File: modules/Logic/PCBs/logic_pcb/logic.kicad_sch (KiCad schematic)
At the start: 14 parts, among them U1 CD74HCT132E, U2 CD74HCT132E, U3 LM324

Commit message: Switch ALU to SMD components
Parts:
- C1: footprint Capacitor_THT:C_Disc_D4.7mm_W2.5mm_P5.00mm -> Capacitor_SMD:C_0805_2012Metric_Pad1.18x1.45mm_HandSolder; JLC (none) -> C376974
- R1, R10, R2, R6, R7, R9: footprint Resistor_THT:R_Axial_DIN0207_L6.3mm_D2.5mm_P10.16mm_Horizontal -> Resistor_SMD:R_0805_2012Metric_Pad1.20x1.40mm_HandSolder; JLC (none) -> C17414
- R3, R4, R5, R8: footprint Resistor_THT:R_Axial_DIN0207_L6.3mm_D2.5mm_P10.16mm_Horizontal -> Resistor_SMD:R_0805_2012Metric_Pad1.20x1.40mm_HandSolder; JLC (none) -> C17513
- U1, U2: footprint Package_DIP:DIP-14_W7.62mm -> Package_SO:SOIC-14_3.9x8.7mm_P1.27mm; JLC (none) -> C484714
- U3: footprint Package_DIP:DIP-14_W7.62mm -> Package_SO:SOIC-14_3.9x8.7mm_P1.27mm; JLC (none) -> C7943
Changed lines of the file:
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@@
 		(shape output)
 		(at 151.13 139.7 0)
-		(fields_autoplaced yes)
 		(effects
 			(font
@@
 		(shape input)
 		(at 38.1 31.75 180)
-		(fields_autoplaced yes)
 		(effects
 			(font
@@
 		(shape output)
 		(at 129.54 95.25 0)
-		(fields_autoplaced yes)
 		(effects
 			(font
@@
 		(shape output)
 		(at 111.76 43.18 0)
-		(fields_autoplaced yes)
 		(effects
 			(font
@@
 		(shape input)
 		(at 92.71 97.79 180)
-		(fields_autoplaced yes)
 		(effects
 			(font
@@
 		(shape input)
 		(at 93.98 118.11 270)
-		(fields_autoplaced yes)
 		(effects
 			(font
@@
 		(shape output)
 		(at 128.27 59.69 0)
-		(fields_autoplaced yes)
 		(effects
 			(font
@@
 		(shape input)
 		(at 38.1 49.53 180)
-		(fields_autoplaced yes)
 		(effects
 			(font
@@
 			)
 		)
-		(property "Footprint" "Resistor_THT:R_Axial_DIN0207_L6.3mm_D2.5mm_P10.16mm_Horizontal"
+		(property "Footprint" "Resistor_SMD:R_0805_2012Metric_Pad1.20x1.40mm_HandSolder"
 			(at 146.05 141.478 90)
 			(effects
@@
 		)
 		(property "Description" "Resistor"
+			(at 146.05 139.7 0)
+			(effects
+				(font
+					(size 1.27 1.27)
+				)
+				(hide yes)
+			)
+		)
+		(property "JLC" "C17513"
 			(at 146.05 139.7 0)
 			(effects
@@
 			)
 		)
-		(property "Footprint" "Package_DIP:DIP-14_W7.62mm"
+		(property "Footprint" "Package_SO:SOIC-14_3.9x8.7mm_P1.27mm"
 			(at 71.12 139.7 0)
 			(effects
@@
 		)
 		(property "Description" "quad 2-input NAND gate"
+			(at 71.12 139.7 0)
+			(effects
+				(font
+					(size 1.27 1.27)
+				)
+				(hide yes)
+			)
+		)
+		(property "JLC" "C484714"
 			(at 71.12 139.7 0)
 			(effects
@@
 			)
 		)
-		(property "Footprint" "Resistor_THT:R_Axial_DIN0207_L6.3mm_D2.5mm_P10.16mm_Horizontal"
+		(property "Footprint" "Resistor_SMD:R_0805_2012Metric_Pad1.20x1.40mm_HandSolder"
 			(at 43.18 33.528 90)
 			(effects
@@
 		)
 		(property "Description" "Resistor"
+			(at 43.18 31.75 0)
+			(effects
+				(font
+					(size 1.27 1.27)
+				)
+				(hide yes)
+			)
+		)
+		(property "JLC" "C17414"
 			(at 43.18 31.75 0)
 			(effects
@@
 			)
 		)
-		(property "Footprint" "Package_DIP:DIP-14_W7.62mm"
+		(property "Footprint" "Package_SO:SOIC-14_3.9x8.7mm_P1.27mm"
 			(at 71.12 34.29 0)
 			(effects
@@
 		)
 		(property "Description" "quad 2-input NAND gate"
+			(at 71.12 34.29 0)
+			(effects
+				(font
+					(size 1.27 1.27)
+				)
+				(hide yes)
+			)
+		)
+		(property "JLC" "C484714"
 			(at 71.12 34.29 0)
 			(effects
@@
 			)
 		)
-		(property "Footprint" "Package_DIP:DIP-14_W7.62mm"
+		(property "Footprint" "Package_SO:SOIC-14_3.9x8.7mm_P1.27mm"
 			(at 110.49 59.69 0)
 			(effects
@@
 		)
 		(property "Description" "quad 2-input NAND gate"
+			(at 110.49 59.69 0)
+			(effects
+				(font
+					(size 1.27 1.27)
+				)
+				(hide yes)
+			)
+		)
+		(property "JLC" "C484714"
 			(at 110.49 59.69 0)
 			(effects
@@
 			)
 		)
-		(property "Footprint" "Package_DIP:DIP-14_W7.62mm"
+		(property "Footprint" "Package_SO:SOIC-14_3.9x8.7mm_P1.27mm"
 			(at 111.76 148.59 0)
 			(effects
@@
 		)
 		(property "Description" "quad 2-input NAND gate"
+			(at 111.76 148.59 0)
+			(effects
+				(font
+					(size 1.27 1.27)
+				)
+				(hide yes)
+			)
+		)
+		(property "JLC" "C484714"
 			(at 111.76 148.59 0)
 			(effects
@@
 			)
 		)
-		(property "Footprint" "Capacitor_THT:C_Disc_D4.7mm_W2.5mm_P5.00mm"
+		(property "Footprint" "Capacitor_SMD:C_0805_2012Metric_Pad1.18x1.45mm_HandSolder"
 			(at 115.57 85.3948 0)
 			(effects
@@
 		)
 		(property "Description" "Unpolarized capacitor"
+			(at 111.76 86.36 0)
+			(effects
+				(font
+					(size 1.27 1.27)
+				)
+				(hide yes)
+			)
+		)
+		(property "JLC" "C376974"
 			(at 111.76 86.36 0)
 			(effects
@@
 			)
 		)
-		(property "Footprint" "Package_DIP:DIP-14_W7.62mm"
+		(property "Footprint" "Package_SO:SOIC-14_3.9x8.7mm_P1.27mm"
 			(at 133.35 139.7 0)
 			(effects
@@
 		)
 		(property "Description" "quad 2-input NAND gate"
+			(at 133.35 139.7 0)
+			(effects
+				(font
+					(size 1.27 1.27)
+				)
+				(hide yes)
+			)
+		)
+		(property "JLC" "C484714"
 			(at 133.35 139.7 0)
 			(effects
@@
 			)
 		)
-		(property "Footprint" "Resistor_THT:R_Axial_DIN0207_L6.3mm_D2.5mm_P10.16mm_Horizontal"
+		(property "Footprint" "Resistor_SMD:R_0805_2012Metric_Pad1.20x1.40mm_HandSolder"
 			(at 123.19 61.468 90)
 			(effects
@@
 		)
 		(property "Description" "Resistor"
+			(at 123.19 59.69 0)
+			(effects
+				(font
+					(size 1.27 1.27)
+				)
+				(hide yes)
+			)
+		)
+		(property "JLC" "C17513"
 			(at 123.19 59.69 0)
 			(effects
@@
 			)
 		)
-		(property "Footprint" "Resistor_THT:R_Axial_DIN0207_L6.3mm_D2.5mm_P10.16mm_Horizontal"
+		(property "Footprint" "Resistor_SMD:R_0805_2012Metric_Pad1.20x1.40mm_HandSolder"
 			(at 124.46 97.028 90)
 			(effects
@@
 		)
 		(property "Description" "Resistor"
+			(at 124.46 95.25 0)
+			(effects
+				(font
+					(size 1.27 1.27)
+				)
+				(hide yes)
+			)
+		)
+		(property "JLC" "C17513"
 			(at 124.46 95.25 0)
 			(effects
@@
 			)
 		)
-		(property "Footprint" "Resistor_THT:R_Axial_DIN0207_L6.3mm_D2.5mm_P10.16mm_Horizontal"
+		(property "Footprint" "Resistor_SMD:R_0805_2012Metric_Pad1.20x1.40mm_HandSolder"
 			(at 95.758 102.87 90)
 			(effects
@@
 		)
 		(property "Description" "Resistor"
+			(at 93.98 102.87 0)
+			(effects
+				(font
+					(size 1.27 1.27)
+				)
+				(hide yes)
+			)
+		)
+		(property "JLC" "C17414"
 			(at 93.98 102.87 0)
 			(effects
@@
 			)
 		)
-		(property "Footprint" "Resistor_THT:R_Axial_DIN0207_L6.3mm_D2.5mm_P10.16mm_Horizontal"
+		(property "Footprint" "Resistor_SMD:R_0805_2012Metric_Pad1.20x1.40mm_HandSolder"
 			(at 111.76 77.978 90)
 			(effects
@@
 		)
 		(property "Description" "Resistor"
+			(at 111.76 76.2 0)
+			(effects
+				(font
+					(size 1.27 1.27)
+				)
+				(hide yes)
+			)
+		)
+		(property "JLC" "C17414"
 			(at 111.76 76.2 0)
 			(effects
@@
 			)
 		)
-		(property "Footprint" "Package_DIP:DIP-14_W7.62mm"
+		(property "Footprint" "Package_SO:SOIC-14_3.9x8.7mm_P1.27mm"
 			(at 92.71 43.18 0)
 			(effects
@@
 		)
 		(property "Description" "quad 2-input NAND gate"
+			(at 92.71 43.18 0)
+			(effects
+				(font
+					(size 1.27 1.27)
+				)
+				(hide yes)
+			)
+		)
+		(property "JLC" "C484714"
 			(at 92.71 43.18 0)
 			(effects
@@
 			)
 		)
-		(property "Footprint" "Resistor_THT:R_Axial_DIN0207_L6.3mm_D2.5mm_P10.16mm_Horizontal"
+		(property "Footprint" "Resistor_SMD:R_0805_2012Metric_Pad1.20x1.40mm_HandSolder"
 			(at 43.18 51.308 90)
 			(effects
@@
 		)
 		(property "Description" "Resistor"
+			(at 43.18 49.53 0)
+			(effects
+				(font
+					(size 1.27 1.27)
+				)
+				(hide yes)
+			)
+		)
+		(property "JLC" "C17414"
 			(at 43.18 49.53 0)
 			(effects
@@
 			)
 		)
-		(property "Footprint" "Package_DIP:DIP-14_W7.62mm"
+		(property "Footprint" "Package_SO:SOIC-14_3.9x8.7mm_P1.27mm"
 			(at 111.76 130.81 0)
 			(effects
@@
 		)
 		(property "Description" "quad 2-input NAND gate"
+			(at 111.76 130.81 0)
+			(effects
+				(font
+					(size 1.27 1.27)
+				)
+				(hide yes)
+			)
+		)
+		(property "JLC" "C484714"
 			(at 111.76 130.81 0)
 			(effects
@@
 			)
 		)
-		(property "Footprint" "Resistor_THT:R_Axial_DIN0207_L6.3mm_D2.5mm_P10.16mm_Horizontal"
+		(property "Footprint" "Resistor_SMD:R_0805_2012Metric_Pad1.20x1.40mm_HandSolder"
 			(at 106.68 44.958 90)
 			(effects
@@
 		)
 		(property "Description" "Resistor"
+			(at 106.68 43.18 0)
+			(effects
+				(font
+					(size 1.27 1.27)
+				)
+				(hide yes)
+			)
+		)
+		(property "JLC" "C17513"
 			(at 106.68 43.18 0)
 			(effects
@@
 			)
 		)
-		(property "Footprint" "Package_DIP:DIP-14_W7.62mm"
+		(property "Footprint" "Package_SO:SOIC-14_3.9x8.7mm_P1.27mm"
 			(at 71.12 52.07 0)
 			(effects
@@
 		)
 		(property "Description" "quad 2-input NAND gate"
+			(at 71.12 52.07 0)
+			(effects
+				(font
+					(size 1.27 1.27)
+				)
+				(hide yes)
+			)
+		)
+		(property "JLC" "C484714"
 			(at 71.12 52.07 0)
 			(effects
@@
 			)
 		)
-		(property "Footprint" "Package_DIP:DIP-14_W7.62mm"
+		(property "Footprint" "Package_SO:SOIC-14_3.9x8.7mm_P1.27mm"
 			(at 110.49 97.79 0)
 			(effects
@@
 		)
 		(property "Description" "Low-Power, Quad-Operational Amplifiers, DIP-14/SOIC-14/SSOP-14"
+			(at 111.76 95.25 0)
+			(effects
+				(font
+					(size 1.27 1.27)
+				)
+				(hide yes)
+			)
+		)
+		(property "JLC" "C7943"
 			(at 111.76 95.25 0)
 			(effects
@@
 			)
 		)
-		(property "Footprint" "Resistor_THT:R_Axial_DIN0207_L6.3mm_D2.5mm_P10.16mm_Horizontal"
+		(property "Footprint" "Resistor_SMD:R_0805_2012Metric_Pad1.20x1.40mm_HandSolder"
 			(at 97.79 94.488 90)
 			(effects
@@
 		)
 		(property "Description" "Resistor"
+			(at 97.79 92.71 0)
+			(effects
+				(font
+					(size 1.27 1.27)
+				)
+				(hide yes)
+			)
+		)
+		(property "JLC" "C17414"
 			(at 97.79 92.71 0)
 			(effects
@@
 			)
 		)
-		(property "Footprint" "Resistor_THT:R_Axial_DIN0207_L6.3mm_D2.5mm_P10.16mm_Horizontal"
+		(property "Footprint" "Resistor_SMD:R_0805_2012Metric_Pad1.20x1.40mm_HandSolder"
 			(at 95.758 113.03 90)
 			(effects
@@
 			(at 93.98 113.03 0)
 			(effects
+				(font
+					(size 1.27 1.27)
+				)
+				(hide yes)
+			)
+		)
+		(property "JLC" "C17414"
+			(at 93.98 113.03 0)
+			(effects

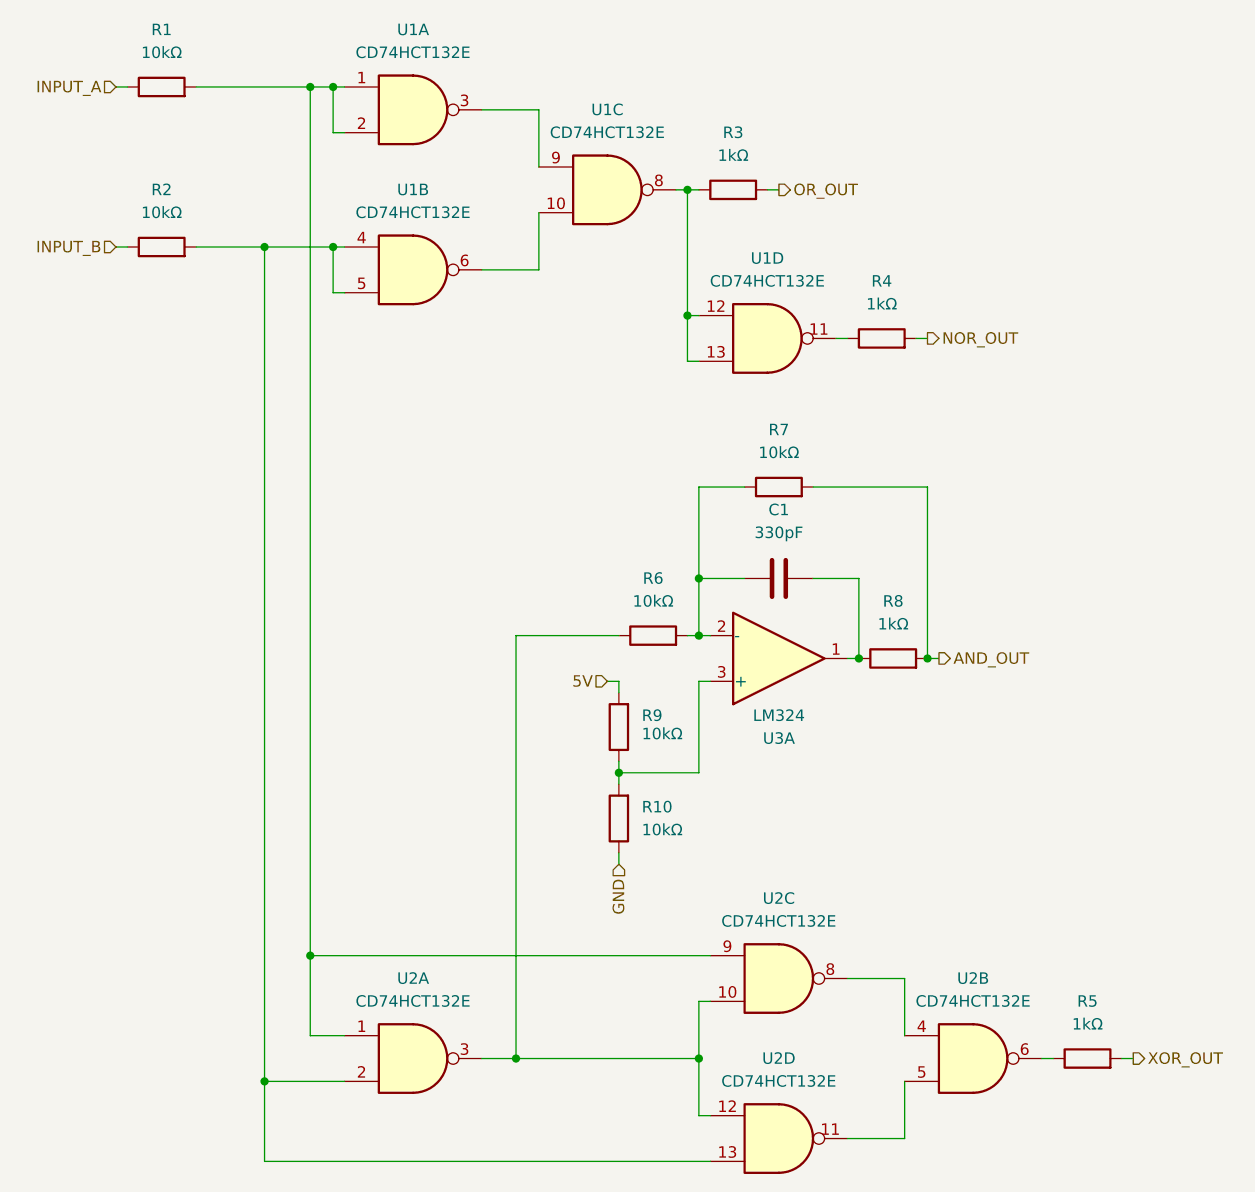
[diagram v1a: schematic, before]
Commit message: [WIP] re-layout back panel to 4hp
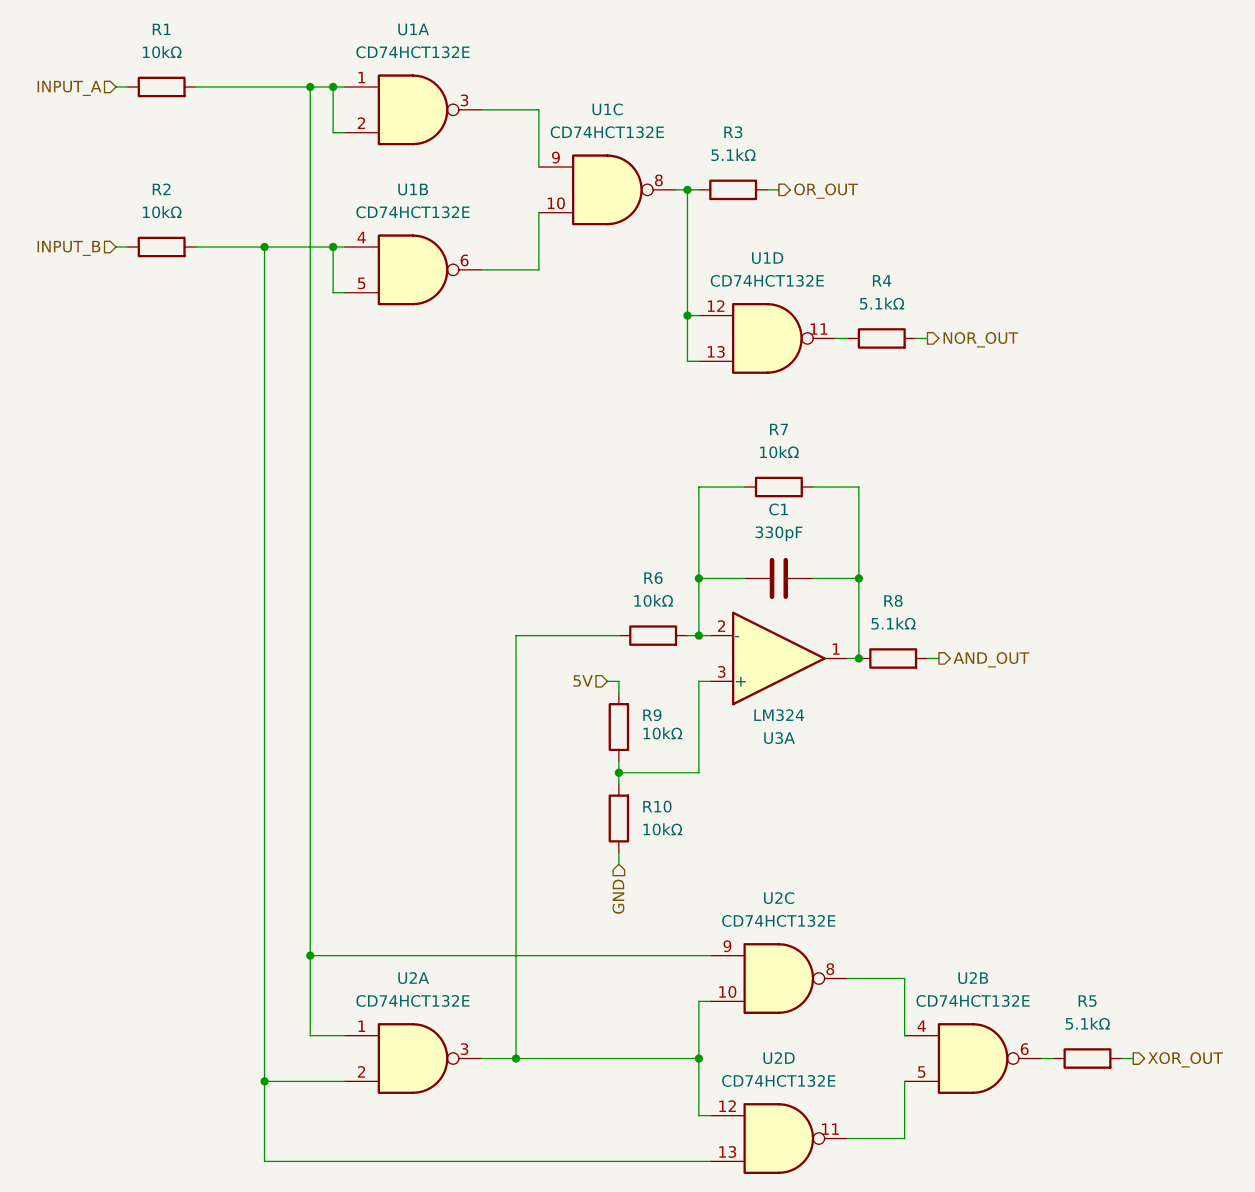
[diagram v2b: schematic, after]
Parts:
- R3, R4, R5, R8: value 1kΩ -> 5.1kΩ; JLC C17513 -> C27834
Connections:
- net AND_OUT: no longer R7.2
- net at C1.2, R8.1, U3.1: now also R7.2
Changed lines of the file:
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@@
-	)
-	(junction
-		(at 128.27 95.25)
-		(diameter 0)
-		(color 0 0 0 0)
 	)
 	(junction
@@
 	)
 	(junction
+		(at 120.65 86.36)
+		(diameter 0)
+		(color 0 0 0 0)
+	)
+	(junction
 		(at 102.87 92.71)
 		(diameter 0)
@@
 	(wire
 		(pts
-			(xy 115.57 76.2) (xy 128.27 76.2)
+			(xy 115.57 76.2) (xy 120.65 76.2)
 		)
 		(stroke
@@
 	(wire
 		(pts
+			(xy 120.65 76.2) (xy 120.65 86.36)
+		)
+		(stroke
+			(width 0)
+			(type default)
+		)
+	)
+	(wire
+		(pts
 			(xy 119.38 59.69) (xy 118.11 59.69)
 		)
@@
 		(pts
 			(xy 93.98 97.79) (xy 93.98 99.06)
-		)
-		(stroke
-			(width 0)
-			(type default)
-		)
-	)
-	(wire
-		(pts
-			(xy 128.27 95.25) (xy 128.27 76.2)
 		)
 		(stroke
@@
 			)
 		)
-		(property "Value" "1kΩ"
+		(property "Value" "5.1kΩ"
 			(at 146.05 135.89 90)
 			(effects
@@
 			)
 		)
-		(property "JLC" "C17513"
+		(property "JLC" "C27834"
 			(at 146.05 139.7 0)
 			(effects
@@
 			)
 		)
-		(property "Value" "1kΩ"
+		(property "Value" "5.1kΩ"
 			(at 123.19 55.88 90)
 			(effects
@@
 			)
 		)
-		(property "JLC" "C17513"
+		(property "JLC" "C27834"
 			(at 123.19 59.69 0)
 			(effects
@@
 			)
 		)
-		(property "Value" "1kΩ"
+		(property "Value" "5.1kΩ"
 			(at 124.46 91.44 90)
 			(effects
@@
 			)
 		)
-		(property "JLC" "C17513"
+		(property "JLC" "C27834"
 			(at 124.46 95.25 0)
 			(effects
@@
 			)
 		)
-		(property "Value" "1kΩ"
+		(property "Value" "5.1kΩ"
 			(at 106.68 39.37 90)
 			(effects
@@
 			)
 		)
-		(property "JLC" "C17513"
+		(property "JLC" "C27834"
 			(at 106.68 43.18 0)
 			(effects

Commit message: Add silkscreen labels to PCB
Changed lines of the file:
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@@
 (kicad_sch
-	(version 20231120)
+	(version 20250114)
 	(generator "eeschema")
-	(generator_version "8.0")
+	(generator_version "9.0")
 	(paper "A4")
 	(junction

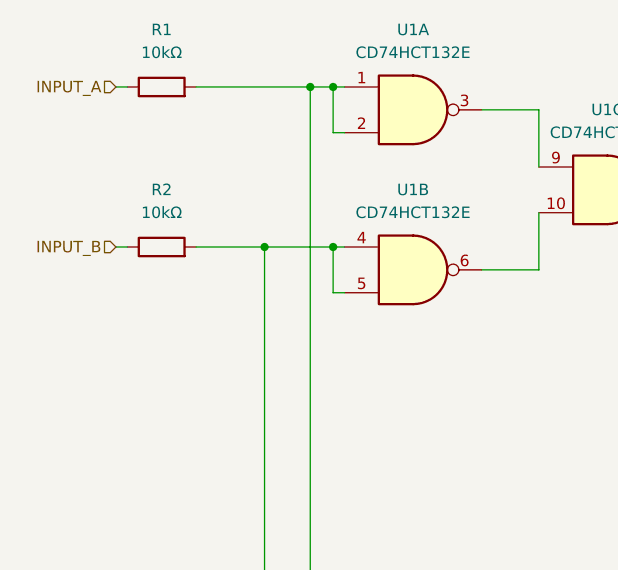
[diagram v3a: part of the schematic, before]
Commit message: Fix wrong pin ordering on logic front; bump both boards to v1.0
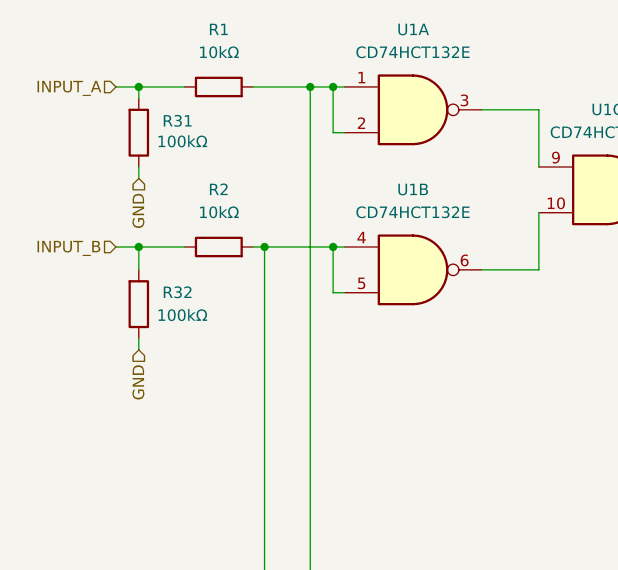
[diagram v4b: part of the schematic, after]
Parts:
- added R31, R32: 100kΩ, Resistor_SMD:R_0805_2012Metric_Pad1.20x1.40mm_HandSolder, symbol Device:R
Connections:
- net GND: now also R31.1, R32.1
- net INPUT_A: now also R31.2
- net INPUT_B: now also R32.2
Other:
- company: (none) -> Free Modular
- title: (none) -> ALU
- moved on the sheet: R1, R2
